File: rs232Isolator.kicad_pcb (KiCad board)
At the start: 2 copper layers, 40 x 30 mm, 30 parts, among them J1 DB9_Male, J2 DB9_Female, U1 MAX3232, U2 6N137, U3 6N137, U4 MAX3232

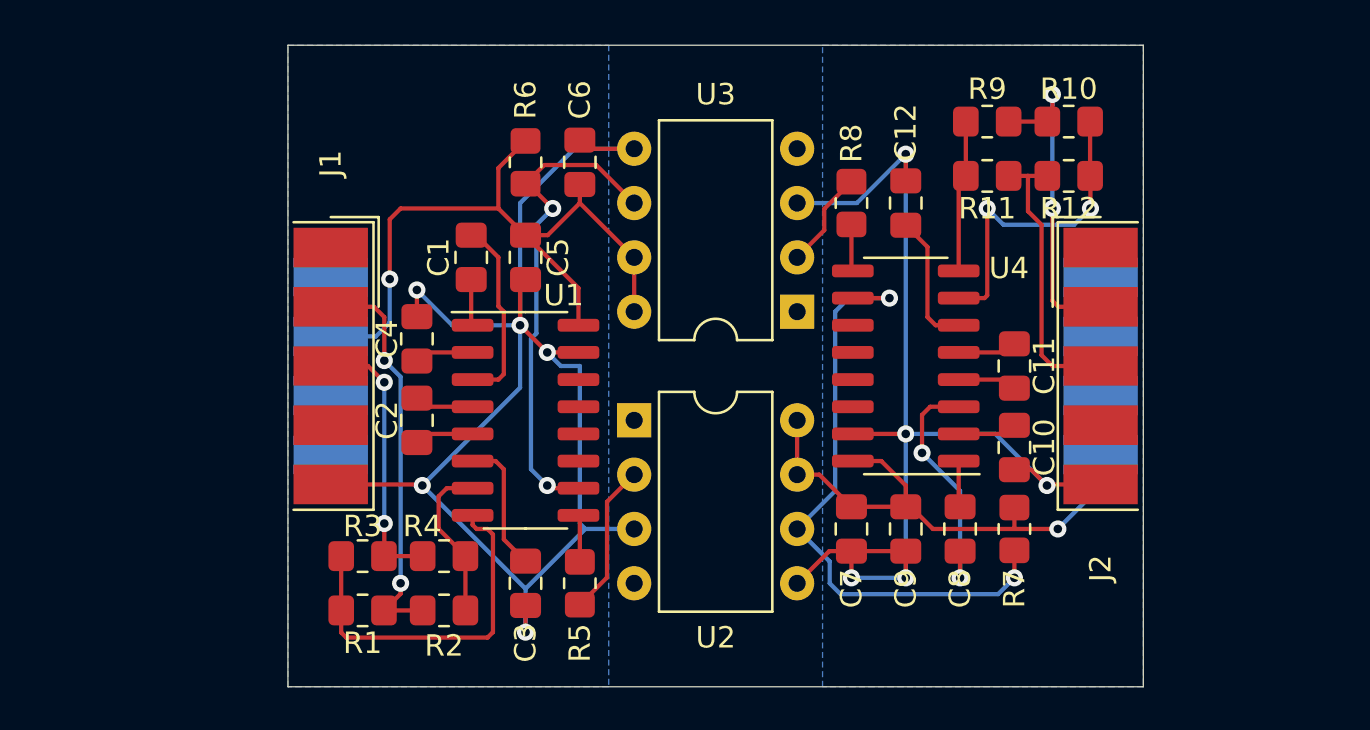
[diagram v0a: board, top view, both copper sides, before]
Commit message: add silkscreen markings and panelization
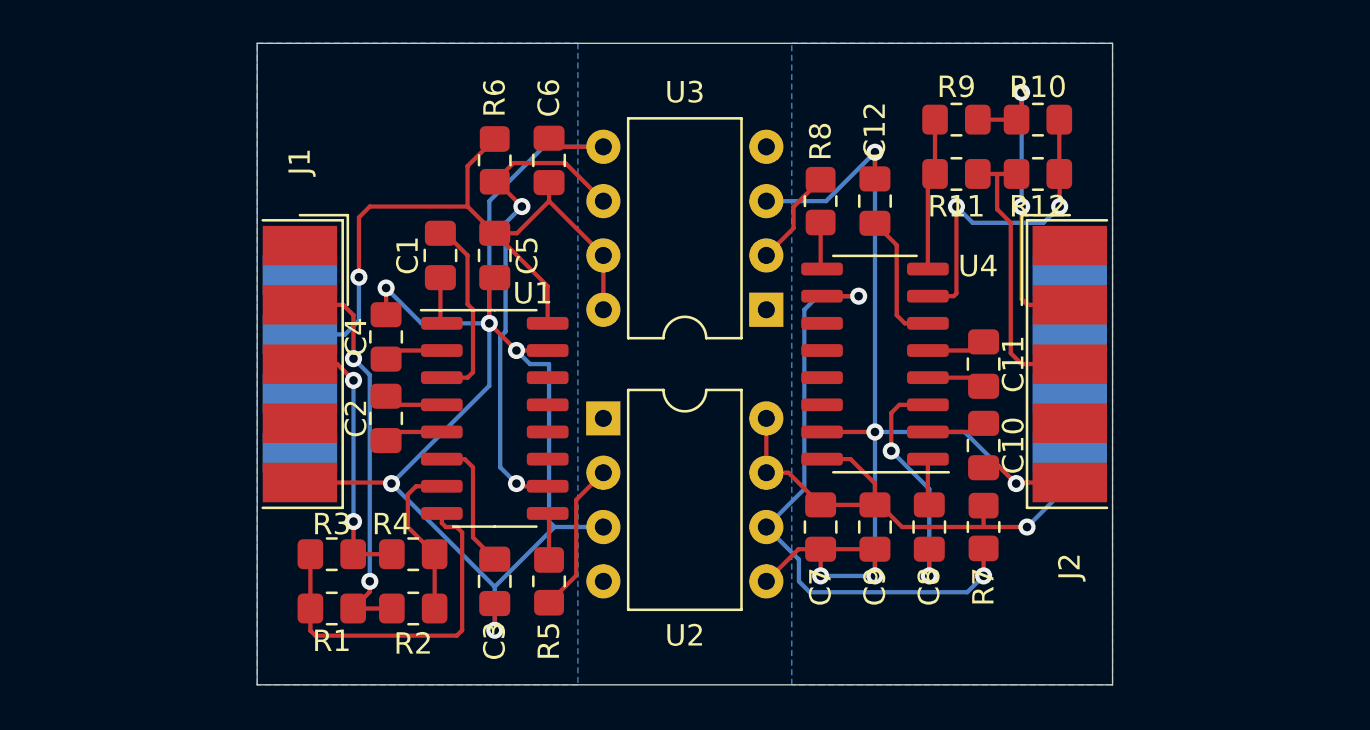
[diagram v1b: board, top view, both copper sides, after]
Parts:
- added G***: LOGO, project:OUR_Logo, B.Cu at (80.0, 85.0)
- moved C1 1.44 mm to (78.6, 79.9)
- moved R3 1.44 mm to (73.5, 93.9)
- moved R8 1.44 mm to (96.3, 77.4)
- moved C7 1.44 mm to (96.3, 92.6)
- moved R1 1.44 mm to (73.5, 96.4)
- moved C10 1.44 mm to (104.0, 88.8)
- moved C11 1.44 mm to (104.0, 85.0)
- moved C12 1.44 mm to (98.9, 77.4)
- moved C3 1.44 mm to (81.1, 95.2)
- moved C5 1.44 mm to (81.1, 79.9)
- moved C6 1.44 mm to (83.7, 75.5)
- moved J1 1.44 mm to (72.0, 85.0)
- moved J2 1.44 mm to (108.0, 85.0)
- moved R10 1.44 mm to (106.5, 73.6)
- moved R11 1.44 mm to (102.7, 76.1)
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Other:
- board text added: "Oxford University Racing RS232 Isolator Rev: A Date: 2020-11-16 Designers: Lance Shi & Andrew Chen"

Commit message: change optocoupler for narrow pcb design
so dsub screws can be used
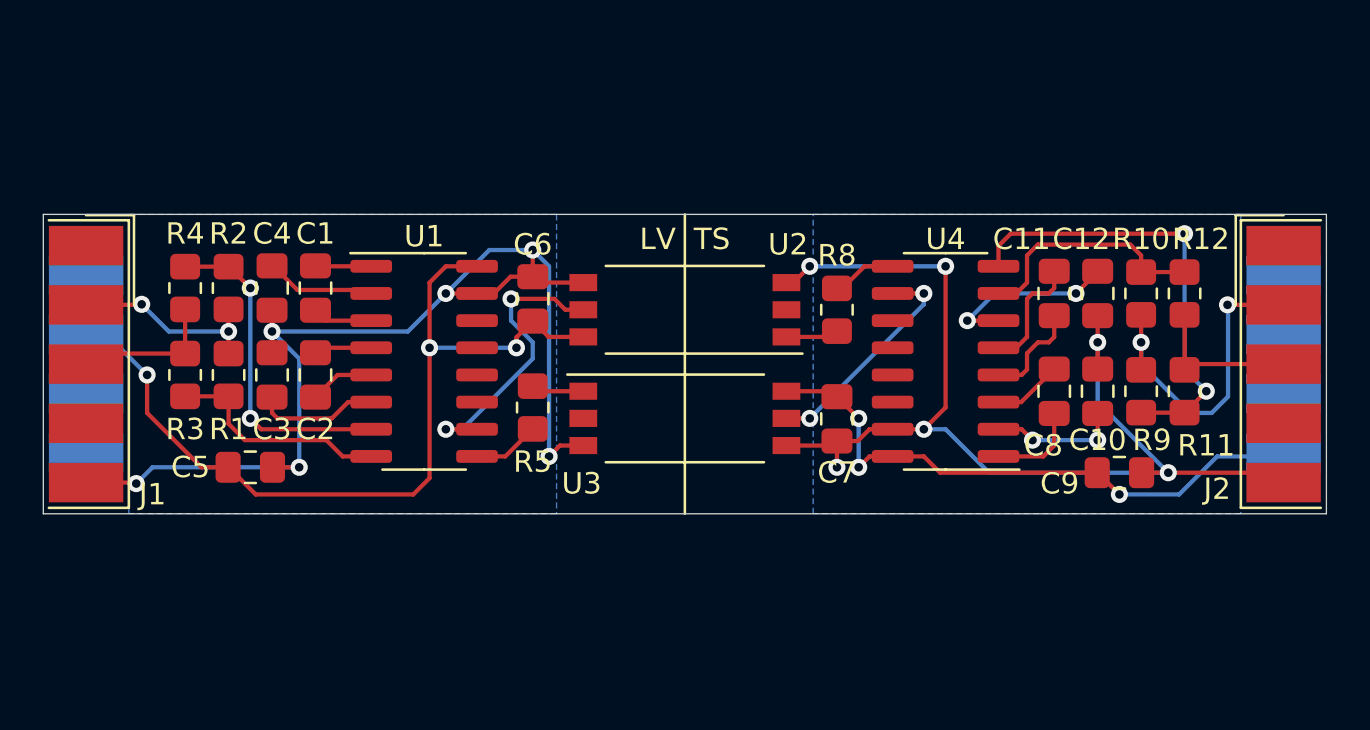
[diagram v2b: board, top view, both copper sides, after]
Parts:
- removed R6, R7: 1000, Resistor_SMD:R_0805_2012Metric_Pad1.20x1.40mm_HandSolder
- R5, R8: value 330 -> 1k
- U2, U3: value 6N137 -> TLP2745; footprint Package_DIP:DIP-8_W7.62mm -> Package_SO:SO-6L_10x3.84mm_P1.27mm
- moved R2 17.3 mm to (68.7, 81.4), turned to 270 degrees
- moved R4 16.4 mm to (66.6, 81.4), turned to 270 degrees
- moved R9 15.4 mm to (111.3, 86.3), turned to 90 degrees
- moved C5 15.1 mm to (69.7, 89.8), turned to 0 degrees
- moved R11 14.7 mm to (113.4, 86.3), turned to 90 degrees
- moved C3 14.2 mm to (70.7, 85.5), turned to 90 degrees
- moved R1 11.9 mm to (68.7, 85.5), turned to 90 degrees
- moved C9 11.7 mm to (110.3, 90.1), turned to 0 degrees
- moved C12 11.3 mm to (109.3, 81.7), turned to 270 degrees
- moved R3 10.8 mm to (66.6, 85.5), turned to 90 degrees
- moved J1 10.0 mm to (62.0, 85.0)
- moved J2 10.0 mm to (118.0, 85.0)
- moved R10 9.45 mm to (111.3, 81.7), turned to 270 degrees
- moved R12 8.85 mm to (113.4, 81.7), turned to 270 degrees
- moved C8 8.63 mm to (107.3, 86.3), turned to 90 degrees
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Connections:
- U1 pad 10: Net-(R6-Pad2) -> Net-(U1-Pad10)
- U2 pad 1: Net-(U2-Pad1) -> Net-(R8-Pad2)
- U2 pad 2: Net-(R5-Pad2) -> Net-(U2-Pad2)
- U2 pad 3: /Gnd1 -> /Gnd2
- U2 pad 4: (no net) -> /Gnd1
- U2 pad 5: /Gnd2 -> Net-(U1-Pad10)
- U2 pad 6: Net-(R7-Pad2) -> /5V1
- U3 pad 1: Net-(U3-Pad1) -> Net-(R5-Pad2)
- U3 pad 2: Net-(R8-Pad2) -> Net-(U3-Pad2)
- U3 pad 3: /Gnd2 -> /Gnd1
- U3 pad 4: (no net) -> /Gnd2
- U3 pad 5: /Gnd1 -> Net-(U3-Pad5)
- U3 pad 6: Net-(R6-Pad2) -> /5V2
- U4 pad 10: Net-(R7-Pad2) -> Net-(U3-Pad5)
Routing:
- net Net-(R7-Pad2): track 29.5 -> 0.00 mm, vias 2 -> 0
- net Net-(R6-Pad2): track 23.5 -> 0.00 mm, vias 2 -> 0
- net /Rx2: track 7.12 -> 21.1 mm, vias 0 -> 2
- net Net-(U1-Pad10): track 0.00 -> 13.7 mm, vias 0 -> 2
- net /Gnd1: track 66.6 -> 54.4 mm, vias 5 -> 6
- net Net-(U3-Pad5): track 0.00 -> 10.6 mm, vias 0 -> 2
- net Net-(J1-Pad2): track 18.9 -> 9.26 mm
- net Net-(C8-Pad2): track 11.5 -> 3.25 mm, vias 2 -> 0
- net /Tx1: track 7.60 -> 15.4 mm, vias 0 -> 2
- net /5V1: track 34.0 -> 41.2 mm, vias 1 -> 3
- net Net-(J2-Pad3): track 13.8 -> 7.32 mm
- net /Rx1: track 17.0 -> 10.6 mm
- net Net-(C1-Pad2): track 8.83 -> 2.81 mm
- net Net-(J1-Pad3): track 12.8 -> 6.92 mm, vias 2 -> 0
- net Net-(R5-Pad2): track 7.13 -> 2.46 mm
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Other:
- board size 40 x 30 mm -> 60 x 14 mm
- board text added: "LV"
- board text added: "TS"
